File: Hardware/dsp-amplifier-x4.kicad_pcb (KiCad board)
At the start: 4 copper layers, 182.5 x 90 mm, 172 parts, among them J1 USBi, J10 Conn_Coaxial, J2 EXT, J3 Raspberry_Pi_2_3, J4 Screw_Terminal_01x02, J5 Screw_Terminal_01x02, J6 Screw_Terminal_01x02, J7 Screw_Terminal_01x02, J8 USB_B, J9 Conn_Coaxial, Q1 STD2805, T1 DA100J, U1 ADAU1452, U10 24LC1025, U2 TPS54308, U3 TPS54308, U4 AMS1117-3.3, U5 SI53365, U6 TAS5760MDCAR, U7 TAS5760MDCAR, U8 USBLC6-2SC6, U9 PCM2707, X1 ASV-24.576MHz-EJ-T, Y1 12 MHz

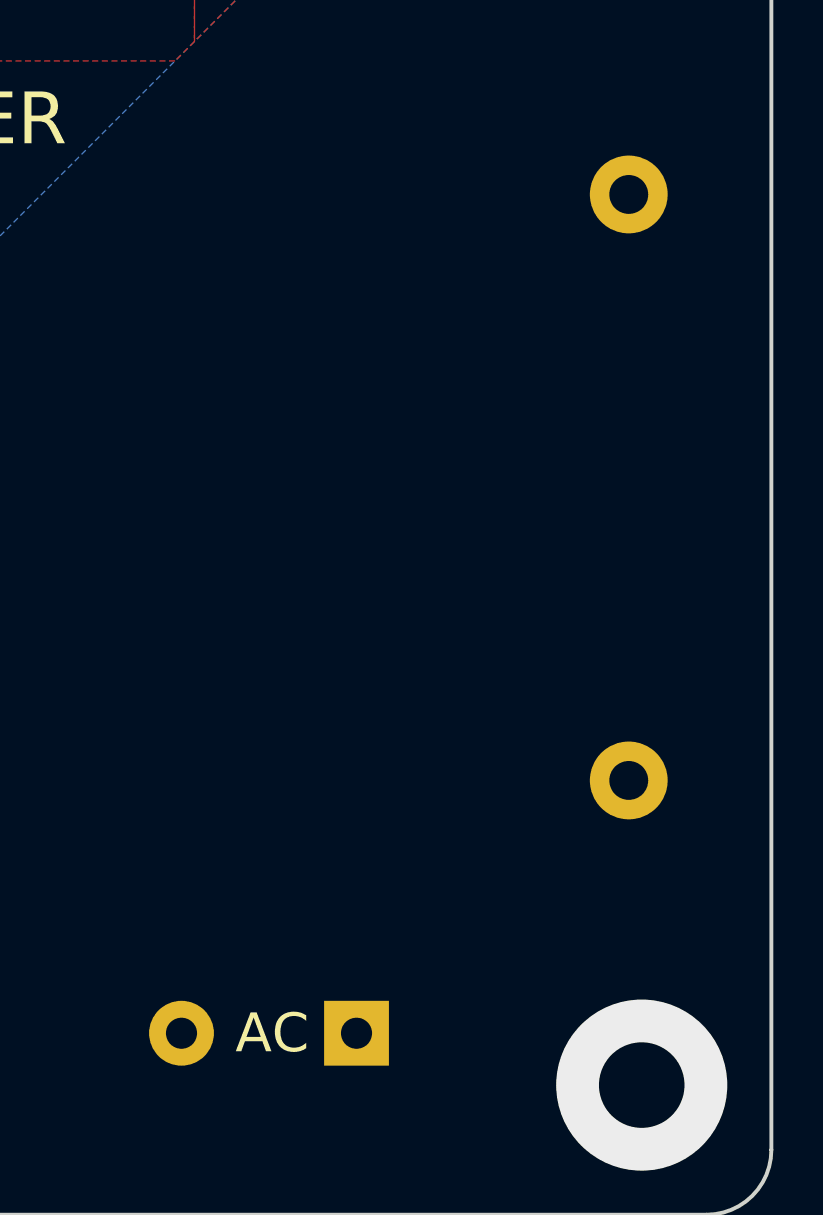
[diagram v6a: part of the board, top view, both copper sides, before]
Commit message: connector for ac
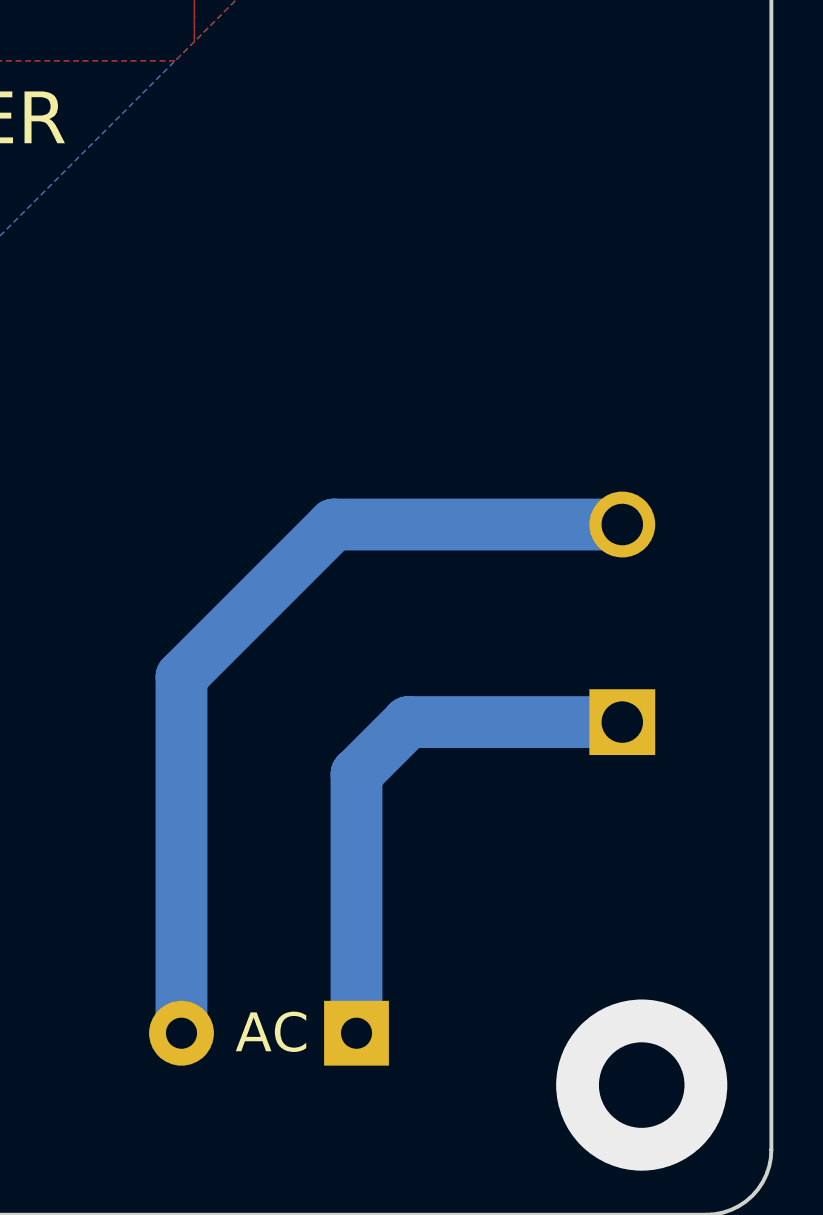
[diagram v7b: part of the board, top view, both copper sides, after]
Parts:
- removed F1: Fuse, Fuse:Fuseholder_Cylinder-5x20mm_Stelvio-Kontek_PTF78_Horizontal_Open
- added P1: Conn_WallPlug, TerminalBlock:TerminalBlock_Wuerth_691311400102_P7.62mm, B.Cu at (236.8, 131.0)
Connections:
- PS1 pad 2: (no net) -> /Power/AC_N
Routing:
- net /Power/AC_N: track 0.00 -> 33.2 mm
- net /Power/AC_L: track 0.00 -> 21.1 mm

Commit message: style fixes, spi/i2c
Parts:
- removed R15, R16, R18: 4.3k, Resistor_SMD:R_0603_1608Metric_Pad0.98x0.95mm_HandSolder
- removed R17, R19: 4.3k DNP, Resistor_SMD:R_0603_1608Metric_Pad0.98x0.95mm_HandSolder
- R14: value 4.3k -> 33
- U10: value 24LC1025 -> 25LCxxx; footprint Package_SO:SO-8_5.3x6.2mm_P1.27mm -> Package_SO:SOIC-8_5.275x5.275mm_P1.27mm
- moved J1 38.7 mm to (103.8, 148.2), turned to 90 degrees
- moved R2 34.1 mm to (99.0, 132.8)
- moved R1 15.3 mm to (105.5, 132.8), turned to 90 degrees
- moved R14 11.5 mm to (103.0, 132.8), turned to 90 degrees
- moved C81 2.76 mm to (107.5, 128.8)
- moved C82 2.76 mm to (109.3, 128.8)
- moved R9 2.69 mm to (127.5, 101.2), turned to 90 degrees
- moved U10 2.15 mm to (113.0, 128.8), turned to 270 degrees
- moved R5 1.50 mm to (125.0, 105.8)
- moved R11 1.41 mm to (124.0, 97.2), turned to 270 degrees
- moved P1 0.50 mm to (236.2, 131.0)
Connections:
- J1 pad 1: /SCL -> (no net)
- J1 pad 3: /SDA -> (no net)
- J1 pad 5: (no net) -> /PI_MISO0
- J1 pad 7: (no net) -> /PI_SCLK0
- J1 pad 8: (no net) -> /PI_MOSI0
- J1 pad 9: (no net) -> /PI_NCE0
- J2 pad 11: /SDA -> (no net)
- J2 pad 13: /SCL -> (no net)
- J3 pad 12: /PI_BCLK -> Net-(J3-Pad12)
- J3 pad 13: (no net) -> /PI_MUTE
- J3 pad 15: (no net) -> /DSP_SELFBOOT
- J3 pad 19: (no net) -> /PI_MOSI0
- J3 pad 21: (no net) -> /PI_MISO0
- J3 pad 22: /DSP_SELFBOOT -> (no net)
- J3 pad 23: (no net) -> /PI_SCLK0
- J3 pad 24: (no net) -> /PI_NCE0
- R14 pad 1: /EEPROM_SCL -> Net-(J3-Pad12)
- R14 pad 2: +3V3 -> /PI_BCLK
- U1 pad 26: /AMP1_NSPK_SD -> /EEPROM_NCS
- U1 pad 27: /AMP1_SPK_SLEEP -> /EEPROM_MOSI
- U1 pad 28: /EEPROM_SCL -> /EEPROM_SCK
- U1 pad 29: /EEPROM_SDA -> /EEPROM_MISO
- U1 pad 30: /SDA -> /PI_MISO0
- U1 pad 31: /SCL -> /PI_SCLK0
- U1 pad 32: /DSP_ADDR1 -> /PI_MOSI0
- U1 pad 33: /DSP_ADDR0 -> /PI_NCE0
- U1 pad 39: (no net) -> /AMP1_NSPK_SD
- U1 pad 42: (no net) -> /AMP1_SPK_SLEEP
- U1 pad 69: (no net) -> /PI_MUTE
- U10 pad 1: +3V3 -> /EEPROM_NCS
- U10 pad 2: +3V3 -> /EEPROM_MISO
- U10 pad 5: /EEPROM_SDA -> /EEPROM_MOSI
- U10 pad 6: /EEPROM_SCL -> /EEPROM_SCK
- U10 pad 7: GND -> +3V3
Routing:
- net /SDA: track 134.4 -> 0.00 mm, vias 2 -> 0
- net /SCL: track 129.9 -> 0.00 mm, vias 2 -> 0
- net /PI_SCLK0: track 0.00 -> 110.1 mm, vias 0 -> 1
- net /PI_MISO0: track 0.00 -> 105.1 mm, vias 0 -> 1
- net /PI_MOSI0: track 0.00 -> 92.1 mm, vias 0 -> 1
- net /PI_NCE0: track 0.00 -> 91.4 mm, vias 0 -> 2
- net /PI_MUTE: track 0.00 -> 55.3 mm, vias 0 -> 2
- net /EEPROM_SCK: track 0.00 -> 26.7 mm, vias 0 -> 2
- net /EEPROM_MOSI: track 0.00 -> 26.3 mm, vias 0 -> 2
- net /DSP_NRESET: track 74.1 -> 50.1 mm, vias 2 -> 1
- net /DSP_SELFBOOT: track 63.6 -> 40.7 mm, vias 2 -> 1
- net /EEPROM_SDA: track 21.8 -> 0.00 mm, vias 2 -> 0
- net /EEPROM_SCL: track 21.6 -> 0.00 mm, vias 2 -> 0
- net /EEPROM_NCS: track 0.00 -> 20.2 mm, vias 0 -> 2
- net /DSP_ADDR1: track 20.1 -> 0.00 mm
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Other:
- board size 182.5 x 90 mm -> 182 x 90 mm
- board text added: "!"
- board text added: "0/0"
- board text added: "0/80"
- board text added: "108/76"
- board text added: "172/0"
- board text added: "172/80"
- board text added: "80/0"
- board text added: "DC/DC"
- board text added: "USBi (SPI)"
- board text removed: "POWER"
- board text removed: "USBi"
